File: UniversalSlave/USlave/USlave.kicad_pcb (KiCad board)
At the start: 2 copper layers, 85 x 71.9 mm, 31 parts, among them J1 Power In, J2 I2C Test Point, J3 ISCP, J4 I2C Through, J5 I2C In, J6 0-3, J7 4-7, J8 8-11, J9 12-15, SW1 Reset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

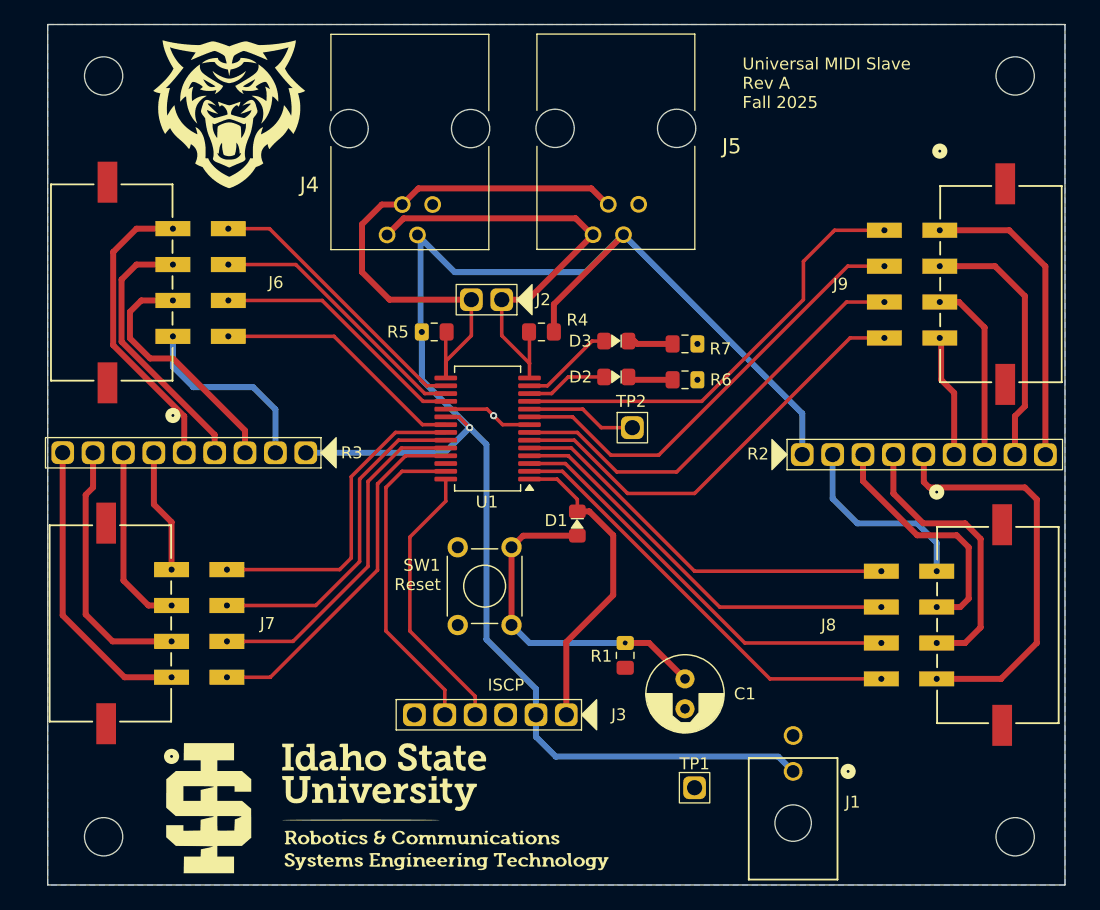
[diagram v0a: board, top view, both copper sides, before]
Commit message: revised IR Tx board
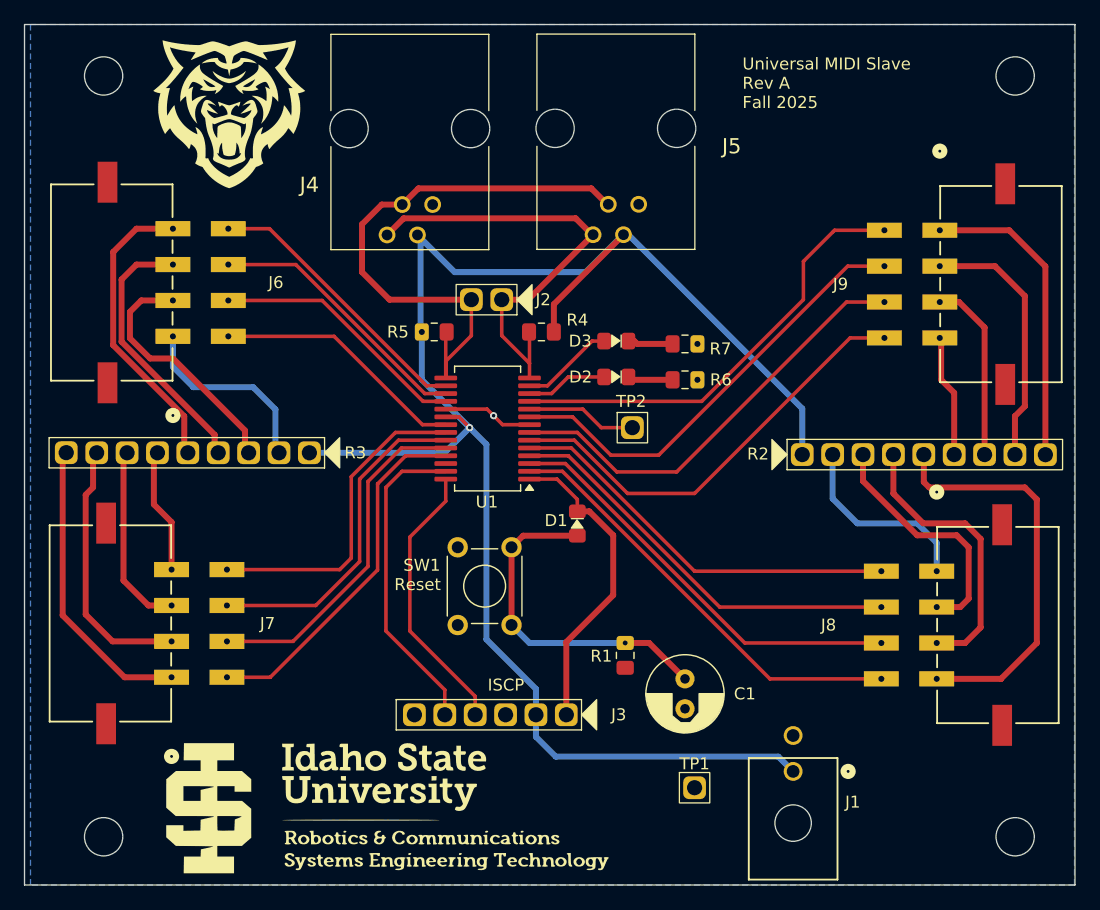
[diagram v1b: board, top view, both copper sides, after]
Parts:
- moved R3 0.30 mm to (160.7, 80.7)
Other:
- board size 85 x 71.9 mm -> 87.8 x 71.9 mm
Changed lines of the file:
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@@
 		(tenting front back)
 		(pcbplotparams
-			(layerselection 0x00000000_00000000_55555555_575555ff)
+			(layerselection 0x00000000_00000000_55555555_5755f5ff)
 			(plot_on_all_layers_selection 0x00000000_00000000_00000000_00000000)
 			(disableapertmacros no)
@@
 	(footprint "2JB_Footprints:1x9_100mil_Header"
 		(layer "F.Cu")
-		(at 160.44 80.67 180)
+		(at 160.74 80.67 180)
 		(property "Reference" "R3"
 			(at -12.7 1.57 0)
@@
 	)
 	(gr_rect
-		(start 147.727461 43.3)
-		(end 232.763998 115.23)
+		(start 145.787461 43.3)
+		(end 233.600999 115.23)
 		(stroke
 			(width 0.1)
@@
 		(layer "F.Fab")
 		(pts
-			(xy 232.492999 43.3) (xy 232.763998 115.23)
+			(xy 232.492999 43.3) (xy 232.492999 115.2)
 		)
 		(height 9.907001)
@@
 			(keep_text_aligned yes)
 		)
-		(gr_text "2.8319"
-			(at 241.3 79.265 90)
+		(gr_text "2.8307"
+			(at 241.3 79.25 90)
 			(layer "F.Fab")
 			(effects
@@
 		(layer "F.Fab")
 		(pts
-			(xy 232.492999 43.3) (xy 147.727461 43.3)
+			(xy 233.6 43.3) (xy 145.8 43.3)
 		)
 		(height -6.6)
@@
 			(keep_text_aligned yes)
 		)
-		(gr_text "3.3372"
-			(at 190.11023 35.55 0)
+		(gr_text "3.4567"
+			(at 189.7 35.55 0)
 			(layer "F.Fab")
 			(effects
@@
 	)
 	(segment
-		(start 210.802999 75.814475)
-		(end 195.857401 60.868877)
+		(start 195.548524 61.151476)
+		(end 192.7 64)
 		(width 0.5)
 		(layer "B.Cu")
@@
 	)
 	(segment
-		(start 195.548524 61.151476)
-		(end 192.7 64)
+		(start 178.9 68.9)
+		(end 179 69)
 		(width 0.5)
 		(layer "B.Cu")
@@
 	)
 	(segment
-		(start 178.9 68.9)
-		(end 179 69)
+		(start 210.802999 75.402999)
+		(end 196.268877 60.868877)
+		(width 0.5)
+		(layer "B.Cu")
+		(net 30)
+	)
+	(segment
+		(start 210.802999 79.25)
+		(end 210.802999 75.402999)
+		(width 0.5)
+		(layer "B.Cu")
+		(net 30)
+	)
+	(segment
+		(start 196.268877 60.868877)
+		(end 195.857401 60.868877)
 		(width 0.5)
 		(layer "B.Cu")
@@
 	)
 	(segment
-		(start 210.802999 79.25)
-		(end 210.802999 75.814475)
-		(width 0.5)
-		(layer "B.Cu")
-		(net 30)
-	)
-	(segment
 		(start 169.3 79.1)
 		(end 180.9 79.1)
@@
 		(polygon
 			(pts
-				(xy 147.727461 43.3) (xy 232.763998 43.3) (xy 232.763998 115.23) (xy 147.727461 115.23)
+				(xy 146.287461 43.3) (xy 233.562999 43.3) (xy 233.562999 115.23) (xy 146.287461 115.23)
 			)
 		)
